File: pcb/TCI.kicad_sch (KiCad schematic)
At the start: 12 parts, among them Q2 DMN3190LDW-7, Q4 STGB20M65DF2

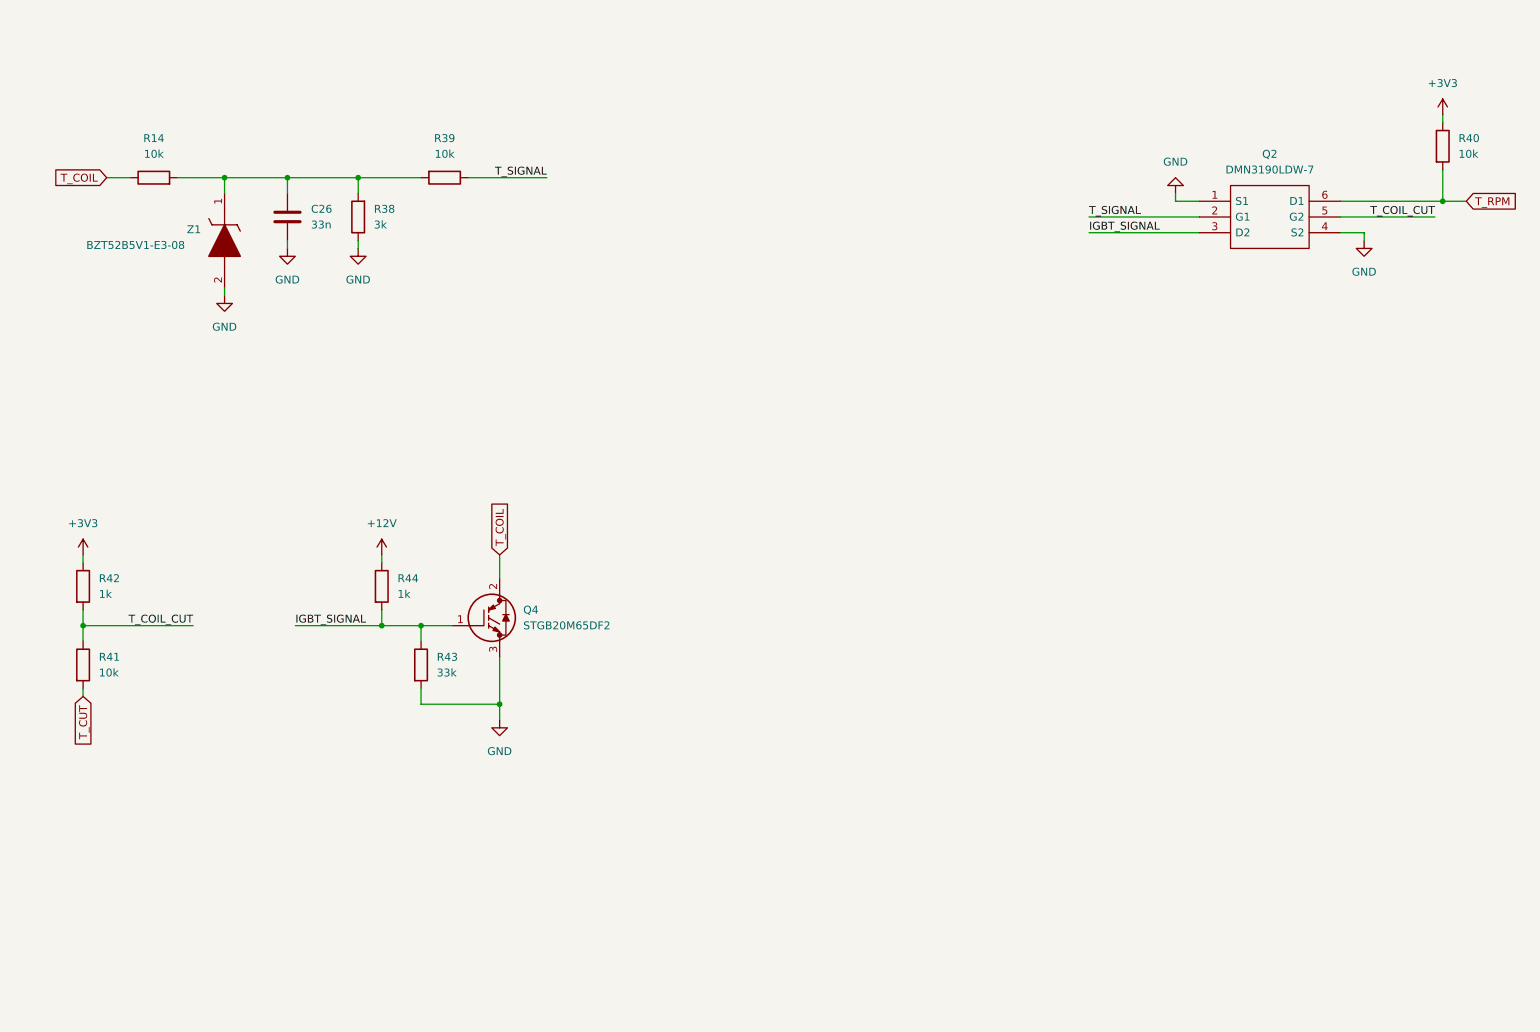
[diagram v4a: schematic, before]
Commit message: widely changed TCI schematic to use a FET IC driver
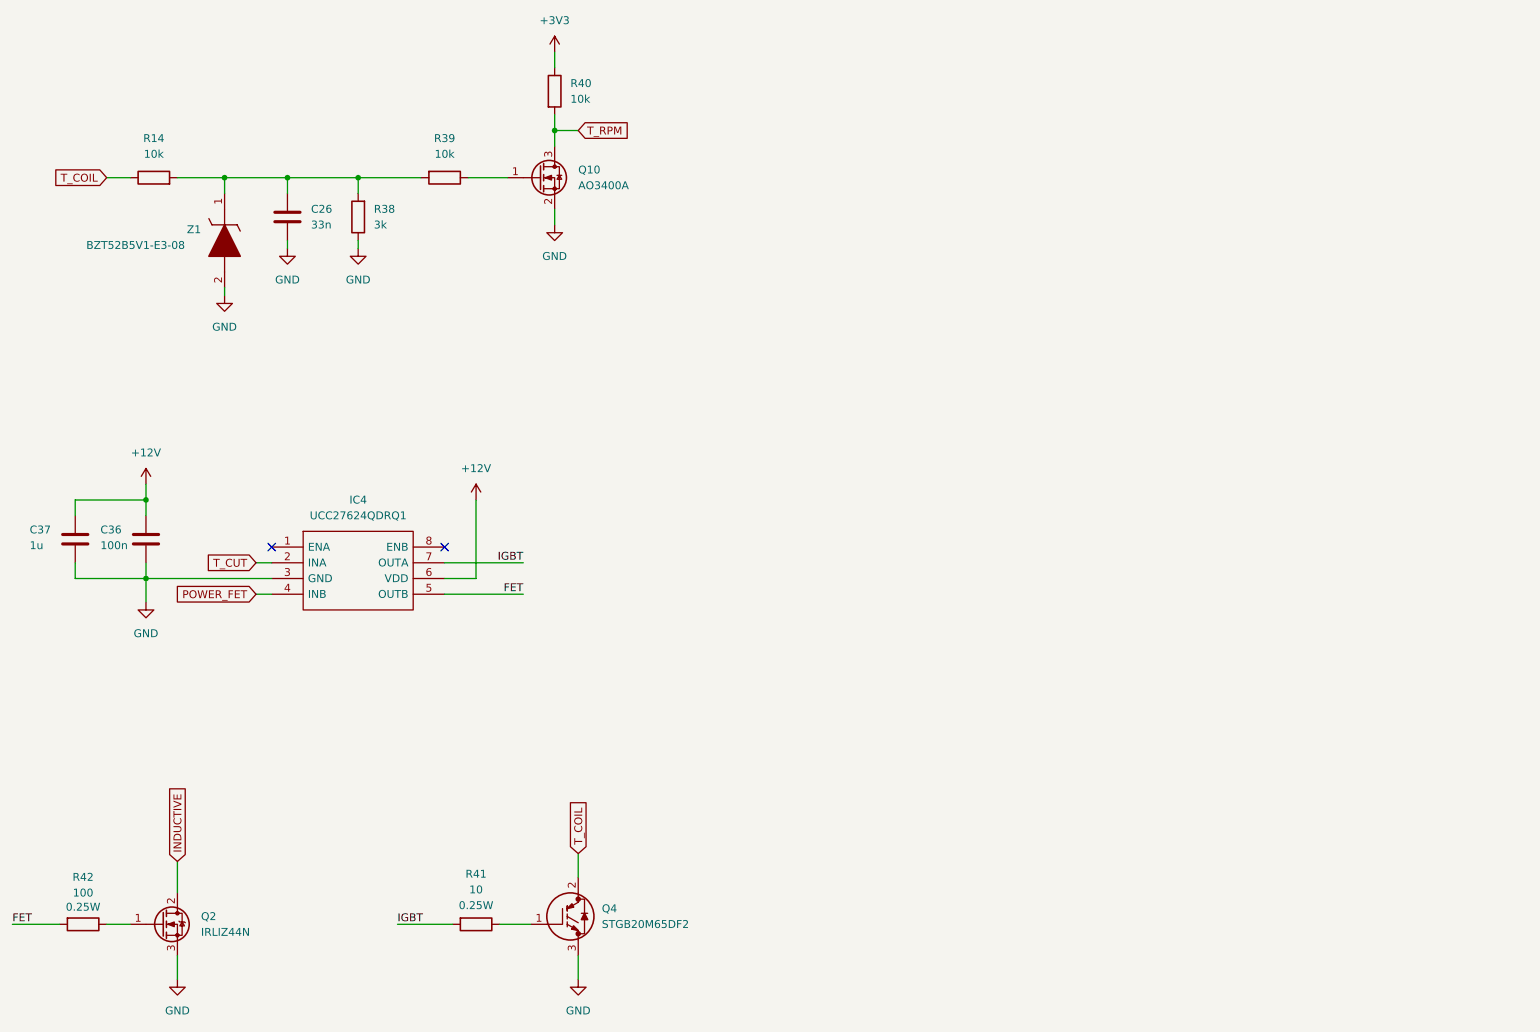
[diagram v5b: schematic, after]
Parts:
- removed Q2: DMN3190LDW-7, SamacSys_Parts:SOT65P210X110-6N, symbol SamacSys_Parts:DMN3190LDW-7
- removed R43: 33k, Resistor_SMD:R_0603_1608Metric, symbol Device:R
- removed R44: 1k, Resistor_SMD:R_0603_1608Metric, symbol Device:R
- added C36: 100n, Capacitor_SMD:C_0603_1608Metric, symbol Device:C
- added C37: 1u, Capacitor_SMD:C_0603_1608Metric, symbol Device:C
- added IC4: UCC27624QDRQ1, SOIC127P600X175-8N, symbol SamacSys_Parts:UCC27624QDRQ1
- added Q10: AO3400A, Package_TO_SOT_SMD:SOT-23, symbol Transistor_FET:AO3400A
- added Q2: IRLIZ44N, Package_TO_SOT_THT:TO-220F-3_Vertical, symbol Transistor_FET:IRLIZ44N
- R41: value 10k -> 10; footprint Resistor_SMD:R_0603_1608Metric -> Resistor_SMD:R_0805_2012Metric
- R42: value 1k -> 100; footprint Resistor_SMD:R_0603_1608Metric -> Resistor_SMD:R_0805_2012Metric
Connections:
- net +12V: now also C36.1, C37.1, IC4.6 (VDD)
- net +3V3: no longer R42.1
- net GND: now also C36.2, C37.2, IC4.3 (GND), Q10.2 (S), Q2.3 (S)
- net T_CUT: now also IC4.2 (INA); no longer R41.2
- net T_RPM: now also Q10.3 (D)
- net IGBT_SIGNAL: no longer names the net of Q4.1
- net IGBT_SIGNAL: now also R41.1
- net T_COIL_CUT renamed FET
- net FET: now also IC4.5 (OUTB); no longer R41.1
- net T_SIGNAL: no longer names the net of R39.1
- net T_SIGNAL: now also Q10.1 (G)
- new net: Q2.1 (G), R42.1
- new net IGBT: IC4.7 (OUTA), R41.2
- new net INDUCTIVE: Q2.2 (D)
- new net POWER_FET: IC4.4 (INB)
- no-connect marks 0 -> 2
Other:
- moved on the sheet: Q4, R40

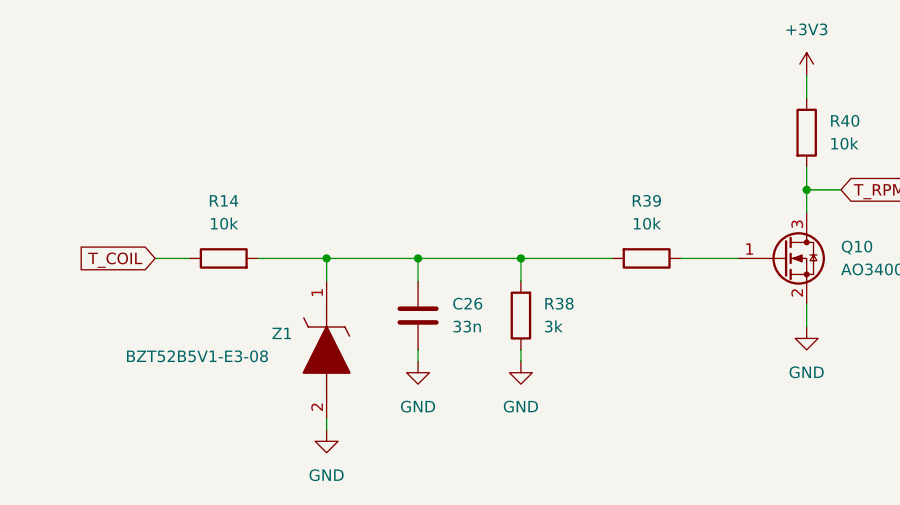
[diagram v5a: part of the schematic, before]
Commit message: added more test points
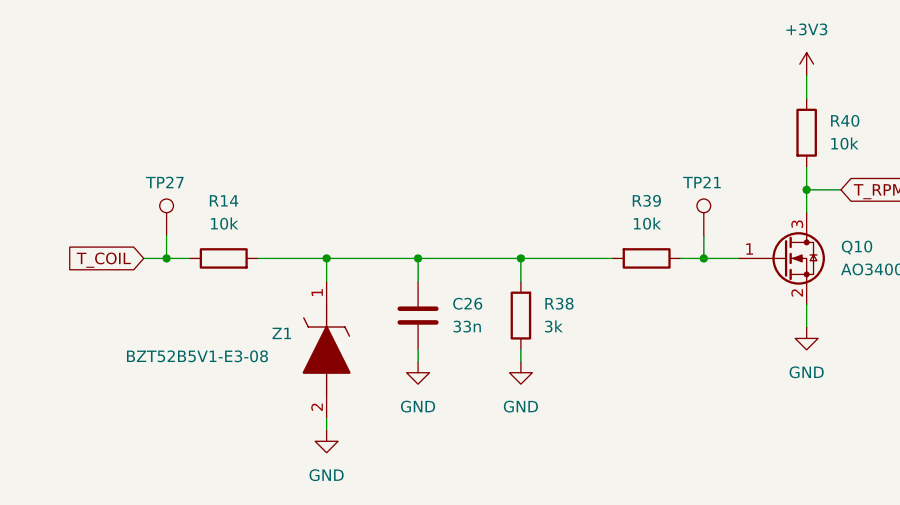
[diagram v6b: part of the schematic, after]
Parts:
- added TP21, TP27: TestPoint, Connector_PinHeader_1.00mm:PinHeader_1x01_P1.00mm_Vertical, symbol Connector:TestPoint
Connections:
- net T_COIL: now also TP27.1
- net at Q10.1 (G), R39.1: now also TP21.1
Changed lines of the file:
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@@
+	)
+	(junction
+		(at 99.06 50.8)
+		(diameter 0)
+		(color 0 0 0 0)
+	)
+	(junction
+		(at 39.37 50.8)
+		(diameter 0)
+		(color 0 0 0 0)
 	)
 	(junction
@@
 	(wire
 		(pts
+			(xy 39.37 48.26) (xy 39.37 50.8)
+		)
+		(stroke
+			(width 0)
+			(type default)
+		)
+	)
+	(wire
+		(pts
 			(xy 33.02 102.87) (xy 44.45 102.87)
 		)
@@
 	(wire
 		(pts
+			(xy 99.06 48.26) (xy 99.06 50.8)
+		)
+		(stroke
+			(width 0)
+			(type default)
+		)
+	)
+	(wire
+		(pts
 			(xy 114.3 176.53) (xy 114.3 180.34)
 		)
@@
 	(wire
 		(pts
-			(xy 41.91 50.8) (xy 38.1 50.8)
+			(xy 41.91 50.8) (xy 39.37 50.8)
 		)
 		(stroke
@@
 	(wire
 		(pts
+			(xy 39.37 50.8) (xy 36.83 50.8)
+		)
+		(stroke
+			(width 0)
+			(type default)
+		)
+	)
+	(wire
+		(pts
 			(xy 110.49 40.64) (xy 110.49 43.18)
 		)
@@
 	(wire
 		(pts
-			(xy 102.87 50.8) (xy 96.52 50.8)
+			(xy 102.87 50.8) (xy 99.06 50.8)
 		)
 		(stroke
@@
 		(pts
 			(xy 44.45 102.87) (xy 44.45 105.41)
+		)
+		(stroke
+			(width 0)
+			(type default)
+		)
+	)
+	(wire
+		(pts
+			(xy 99.06 50.8) (xy 96.52 50.8)
 		)
 		(stroke
@@
 	(global_label "T_COIL"
 		(shape input)
-		(at 38.1 50.8 180)
+		(at 36.83 50.8 180)
 		(fields_autoplaced yes)
 		(effects
@@
 		)
 		(property "Intersheetrefs" "${INTERSHEET_REFS}"
-			(at 28.9462 50.8 0)
+			(at 27.6762 50.8 0)
 			(effects
 				(font
@@
 					(unit 1)
 				)
+			)
+		)
+	)
+	(symbol
+		(lib_id "Connector:TestPoint")
+		(at 99.06 48.26 0)
+		(unit 1)
+		(exclude_from_sim no)
+		(in_bom yes)
+		(on_board yes)
+		(dnp no)
+		(property "Reference" "TP21"
+			(at 96.774 42.418 0)
+			(effects
+				(font
+					(size 1.27 1.27)
+				)
+				(justify left)
+			)
+		)
+		(property "Value" "TestPoint"
+			(at 101.6 46.2279 0)
+			(effects
+				(font
+					(size 1.27 1.27)
+				)
+				(justify left)
+				(hide yes)
+			)
+		)
+		(property "Footprint" "Connector_PinHeader_1.00mm:PinHeader_1x01_P1.00mm_Vertical"
+			(at 104.14 48.26 0)
+			(effects
+				(font
+					(size 1.27 1.27)
+				)
+				(hide yes)
+			)
+		)
+		(property "Datasheet" "~"
+			(at 104.14 48.26 0)
+			(effects
+				(font
+					(size 1.27 1.27)
+				)
+				(hide yes)
+			)
+		)
+		(property "Description" "test point"
+			(at 99.06 48.26 0)
+			(effects
+				(font
+					(size 1.27 1.27)
+				)
+				(hide yes)
+			)
+		)
+		(pin "1"
+		)
+		(instances
+			(project "ecu-dev-board"
+				(path "/38d4df77-b5a0-4642-8410-8b13c21c2c3b/1f135221-d921-46ea-b769-b97fce3b730c"
+					(reference "TP21")
+					(unit 1)
+				)
+			)
+		)
+	)
+	(symbol
+		(lib_id "Connector:TestPoint")
+		(at 39.37 48.26 0)
+		(unit 1)
+		(exclude_from_sim no)
+		(in_bom yes)
+		(on_board yes)
+		(dnp no)
+		(property "Reference" "TP27"
+			(at 37.084 42.418 0)
+			(effects
+				(font
+					(size 1.27 1.27)
+				)
+				(justify left)
+			)
+		)
+		(property "Value" "TestPoint"
+			(at 41.91 46.2279 0)
+			(effects
+				(font
+					(size 1.27 1.27)
+				)
+				(justify left)
+				(hide yes)
+			)
+		)
+		(property "Footprint" "Connector_PinHeader_1.00mm:PinHeader_1x01_P1.00mm_Vertical"
+			(at 44.45 48.26 0)
+			(effects
+				(font
+					(size 1.27 1.27)
+				)
+				(hide yes)
+			)
+		)
+		(property "Datasheet" "~"
+			(at 44.45 48.26 0)
+			(effects
+				(font
+					(size 1.27 1.27)
+				)
+				(hide yes)
+			)
+		)
+		(property "Description" "test point"
+			(at 39.37 48.26 0)
+			(effects
+				(font
+					(size 1.27 1.27)
+				)
+				(hide yes)
+			)
+		)
+		(pin "1"
+		)
+		(instances
+			(project "ecu-dev-board"
+				(path "/38d4df77-b5a0-4642-8410-8b13c21c2c3b/1f135221-d921-46ea-b769-b97fce3b730c"
+					(reference "TP27")
+					(unit 1)
+				)

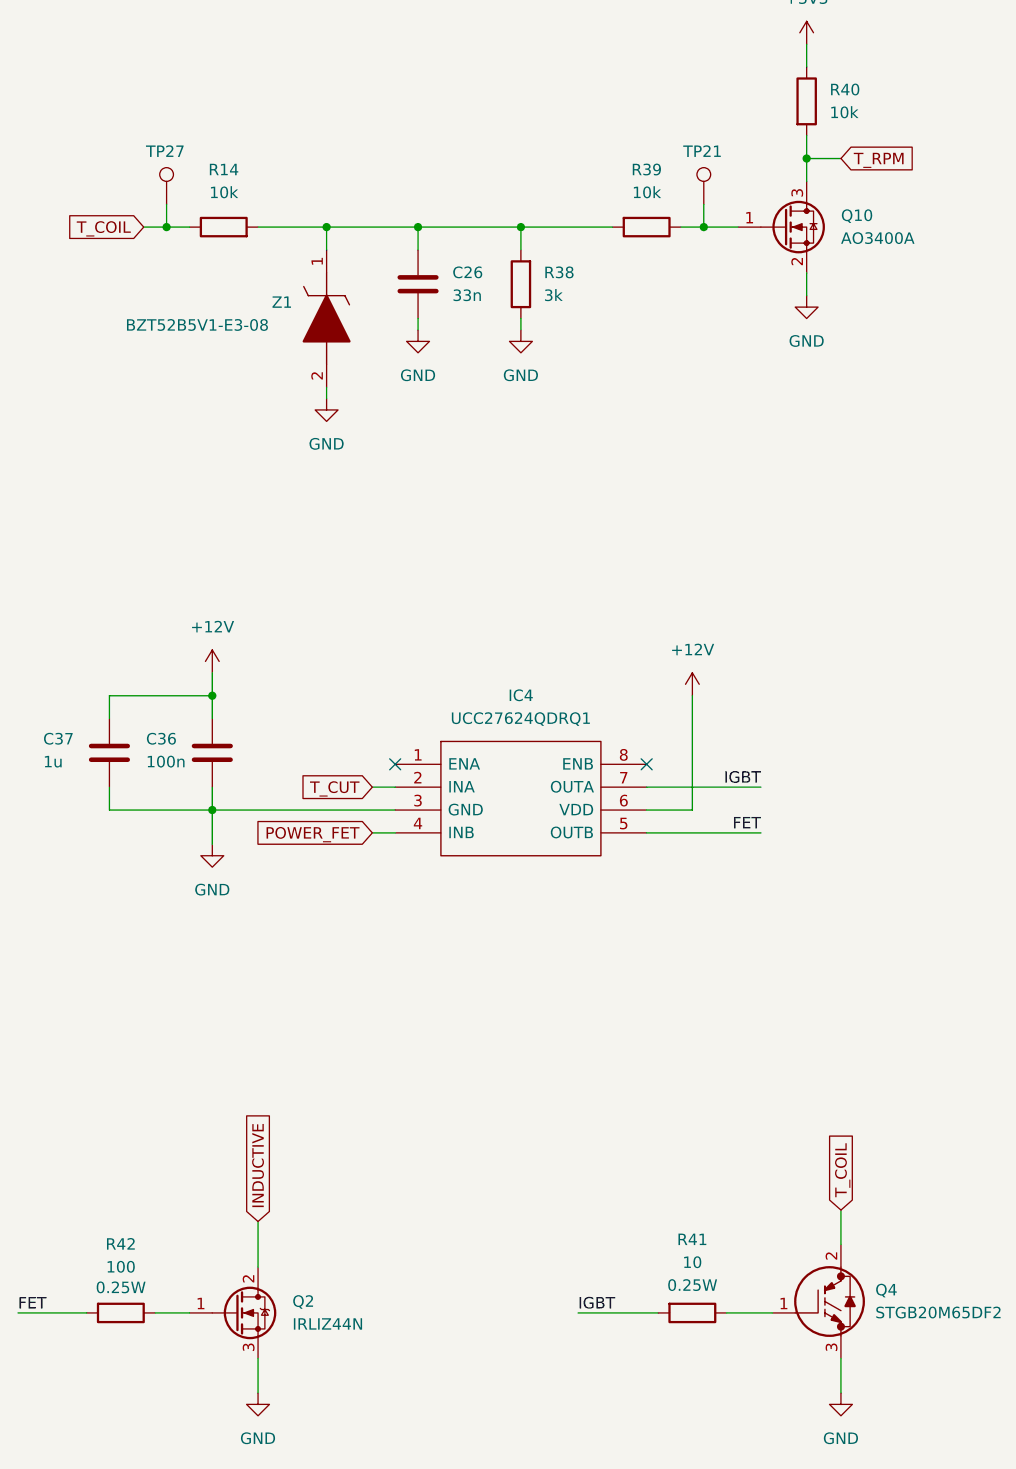
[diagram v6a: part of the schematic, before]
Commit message: added DNP for fabrication and 2P molex connector, minor fixes
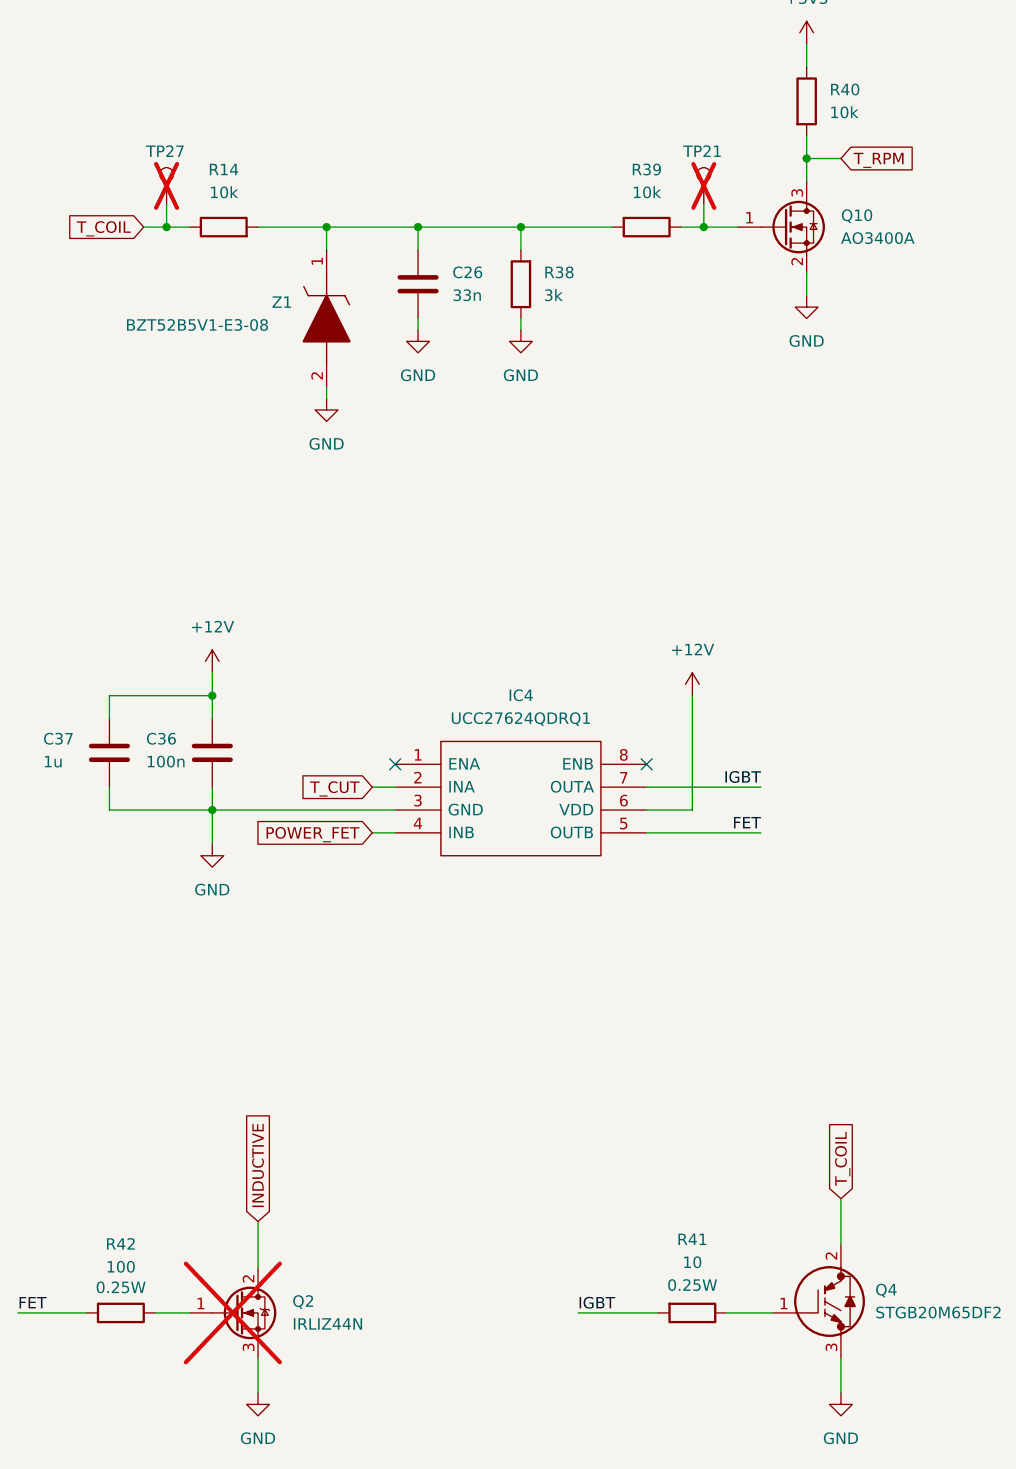
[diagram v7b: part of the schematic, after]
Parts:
- IC4: footprint SOIC127P600X175-8N -> SamacSys_Parts:SOIC127P600X175-8N
- Q2: now not fitted
- TP21, TP27: footprint Connector_PinHeader_1.00mm:PinHeader_1x01_P1.00mm_Vertical -> Connector_PinHeader_2.54mm:PinHeader_1x01_P2.54mm_Vertical; now not fitted
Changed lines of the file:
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@@
+	(wire
+		(pts
+			(xy 114.3 158.75) (xy 114.3 163.83)
+		)
+		(stroke
+			(width 0)
+			(type default)
+		)
+	)
 	(wire
 		(pts
@@
 		(pts
 			(xy 105.41 118.11) (xy 92.71 118.11)
-		)
-		(stroke
-			(width 0)
-			(type default)
-		)
-	)
-	(wire
-		(pts
-			(xy 114.3 160.02) (xy 114.3 163.83)
 		)
 		(stroke
@@
 	(global_label "T_COIL"
 		(shape input)
-		(at 114.3 160.02 90)
+		(at 114.3 158.75 90)
 		(fields_autoplaced yes)
 		(effects
@@
 		)
 		(property "Intersheetrefs" "${INTERSHEET_REFS}"
-			(at 114.3 150.8662 90)
+			(at 114.3 149.5962 90)
 			(effects
 				(font
@@
 		(in_bom yes)
 		(on_board yes)
-		(dnp no)
+		(dnp yes)
 		(property "Reference" "TP21"
 			(at 96.774 42.418 0)
@@
 			)
 		)
-		(property "Footprint" "Connector_PinHeader_1.00mm:PinHeader_1x01_P1.00mm_Vertical"
+		(property "Footprint" "Connector_PinHeader_2.54mm:PinHeader_1x01_P2.54mm_Vertical"
 			(at 104.14 48.26 0)
 			(effects
@@
 		(in_bom yes)
 		(on_board yes)
-		(dnp no)
+		(dnp yes)
 		(property "Reference" "TP27"
 			(at 37.084 42.418 0)
@@
 			)
 		)
-		(property "Footprint" "Connector_PinHeader_1.00mm:PinHeader_1x01_P1.00mm_Vertical"
+		(property "Footprint" "Connector_PinHeader_2.54mm:PinHeader_1x01_P2.54mm_Vertical"
 			(at 44.45 48.26 0)
 			(effects
@@
 		(in_bom yes)
 		(on_board yes)
-		(dnp no)
+		(dnp yes)
 		(fields_autoplaced yes)
 		(property "Reference" "Q2"
@@
 			)
 		)
-		(property "Footprint" "SOIC127P600X175-8N"
+		(property "Footprint" "SamacSys_Parts:SOIC127P600X175-8N"
 			(at 88.9 107.95 0)
 			(effects

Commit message: changed zener footprints
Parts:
- Z1: footprint SamacSys_Parts:BZT52B5V1E308 -> Diode_SMD:D_SOD-123
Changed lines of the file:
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@@
 			)
 		)
-		(property "Footprint" "SamacSys_Parts:BZT52B5V1E308"
+		(property "Footprint" "Diode_SMD:D_SOD-123"
 			(at 60.96 63.5 0)
 			(effects
